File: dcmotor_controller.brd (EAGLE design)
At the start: 142.2 x 90.6 mm, 87 parts, among them IC1 L298, IC2 L298, Q1 MOSFET-PCHANNEL_SOT23-3, Q2 8MHz, T1 BC857BS, T14 BSS306N, U1 SN74LVC4245APWR, U2 STM32F10XRXT6, U3 SN74LVC4245APWR, U4 MCP1825S-3302E/DB

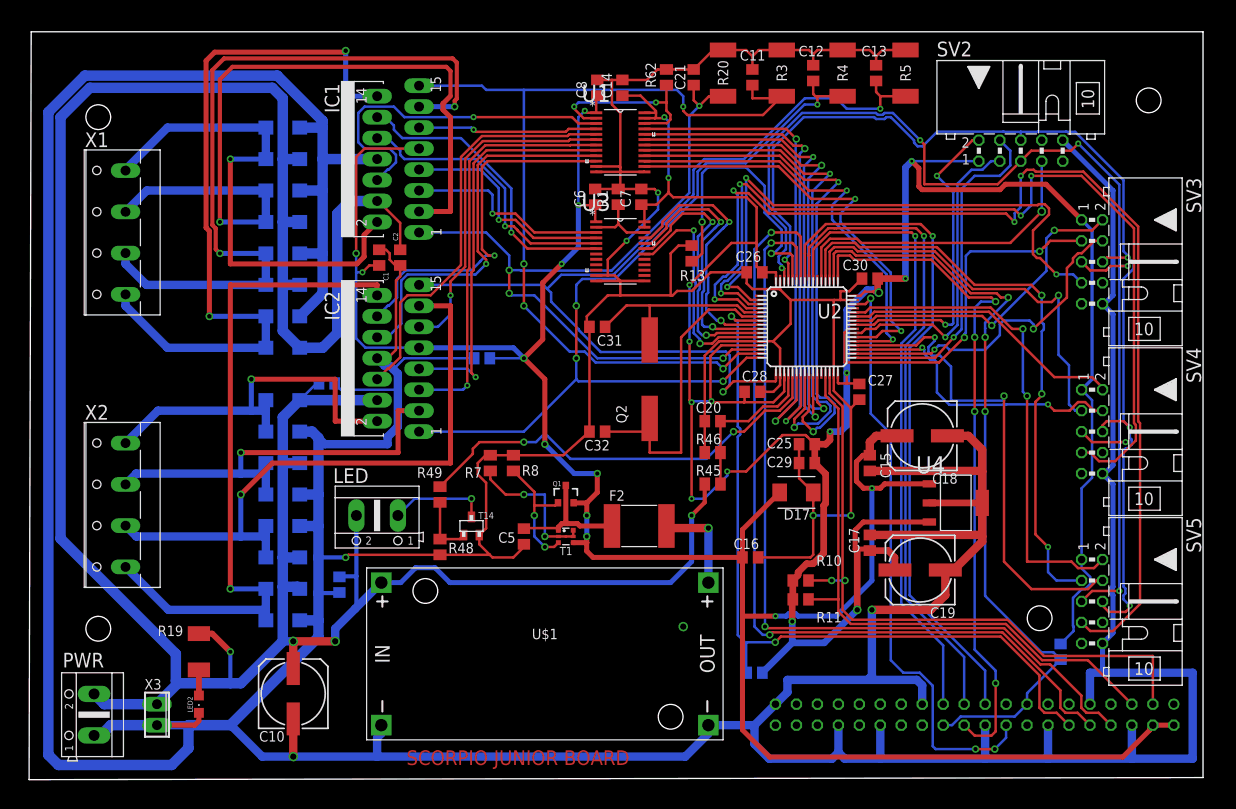
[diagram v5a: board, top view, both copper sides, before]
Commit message: renumber parts, small changes in layout
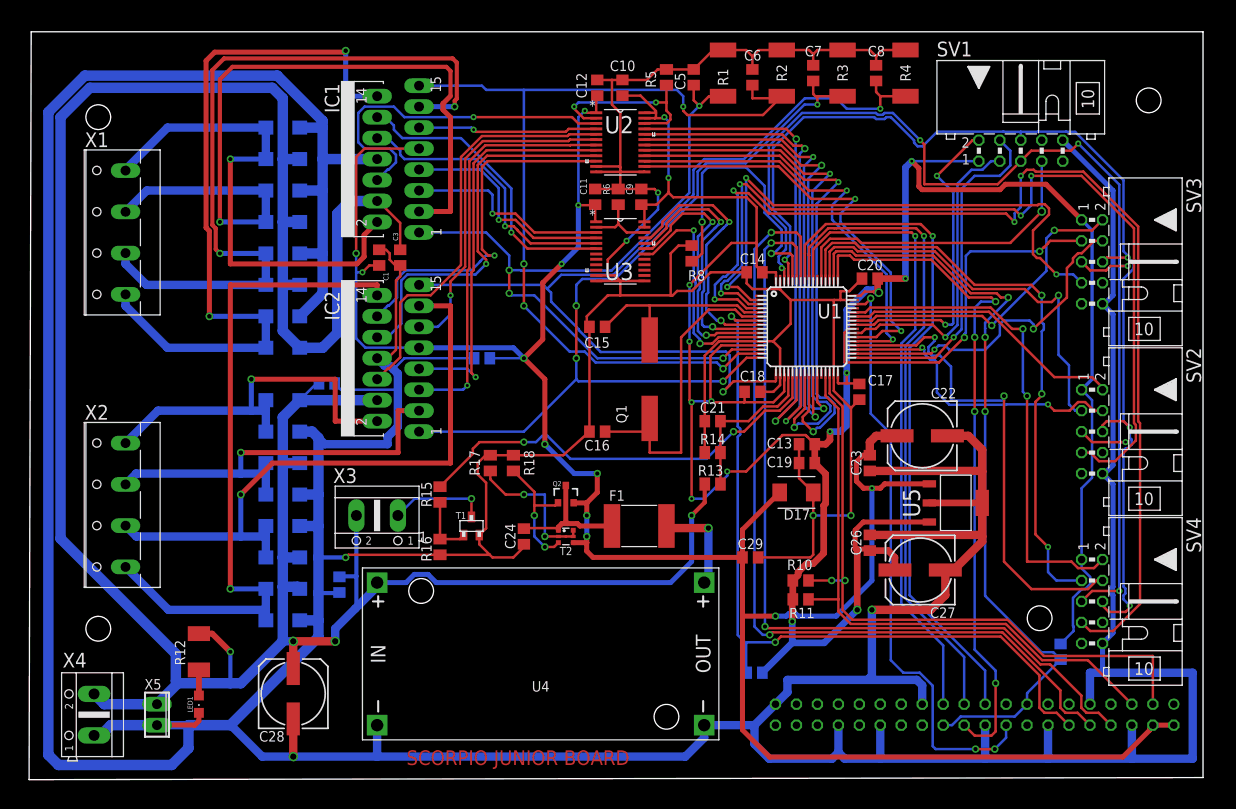
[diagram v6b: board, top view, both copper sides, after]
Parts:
- removed C30: 100n, rcl:C0805
- removed C31, C32: 20p, rcl:C0805
- removed LED: (no value), con-ptr500:AK500/2
- removed R19: 1.2k, 0.5W, rcl:R2010
- removed R20: 0R25, rcl:R2512
- removed R45, R62: 10k, resistor:M0805
- removed R46: 2k2, resistor:M0805
- removed SV6: (no value), con-lsta:FE20-2
- removed T14: BSS306N, we-transistor:SOT23
- removed U$1: DC-DC-STEP-DOWN-LM2596, lm2596:DC-DC-STEP-DOWN-LM2596
- added C22: 10u, resistor:153CLV-0807
- added C23: 100n, resistor:C0805
- added C24: (no value), rcl:C0805
- added R17, R18: 10k 1%, resistor:M0805
- added R2: 0R25, rcl:R2512
- added R6: 10k, resistor:M0805
- added R9: (no value), rcl:R0805
- added SV1: (no value), con-ml:ML10L
- added T2: BC857BS, NXP_60_26022015:SOT363
- added U5: MCP1825S-3302E/DB, MCP1825S-3302E_DB:SOT230P700X180-4N
- added X5: (no value), con-phoenix-254:2POL254
- C10: value 100u -> 100n; device resistor:153CLV-0807 -> resistor:C0805
- C13: value 100n -> 4u7; device resistor:C0805 -> rcl:C0805
- C14, C17, C3: device resistor:C0805 -> rcl:C0805
- C15, C16: value 100n -> 20p; device resistor:C0805 -> rcl:C0805
- C18: value 10u -> 100n; device resistor:153CLV-0807 -> rcl:C0805
- C19: value 10u -> 1u; device resistor:153CLV-0807 -> rcl:C0805
- C2, C25, C26: device rcl:C0805 -> resistor:C0805
- C20: value 47u -> 100n; device resistor:C0805 -> rcl:C0805
- C21: value 100n -> 47u
- C27: value 100n -> 10u; device rcl:C0805 -> resistor:153CLV-0807
- C28: value 100n -> 100u; device rcl:C0805 -> resistor:153CLV-0807
- C29: value 1u -> 100n; device rcl:C0805 -> resistor:C0805
- C5: value (none) -> 100n; device rcl:C0805 -> resistor:C0805
- C9: value 4u7 -> 100n
- Q1: value MOSFET-PCHANNEL_SOT23-3 -> 8MHz; device Simplex-DiscreteSemi:SOT23-3 -> crystal:CSM-7X-DU
- Q2: value 8MHz -> MOSFET-PCHANNEL_SOT23-3; device crystal:CSM-7X-DU -> Simplex-DiscreteSemi:SOT23-3
- R1: value 10k -> 0R25; device resistor:M0805 -> rcl:R2512
- R12: value 10k -> 1.2k, 0.5W; device rcl:R0805 -> rcl:R2010
- R13: device rcl:R0805 -> resistor:M0805
- R14: value (none) -> 2k2; device rcl:R0805 -> resistor:M0805
- R5: value 0R25 -> 10k; device rcl:R2512 -> resistor:M0805
- R7, R8: value 10k 1% -> 10k; device resistor:M0805 -> rcl:R0805
- SV5: device con-ml:ML10L -> con-lsta:FE20-2
- T1: value BC857BS -> BSS306N; device NXP_60_26022015:SOT363 -> we-transistor:SOT23
- U1: value SN74LVC4245APWR -> STM32F10XRXT6; device Texas Instruments_By_element14_Batch_1:SOP65P640X120-24N -> stm32:TQFP64
- U2: value STM32F10XRXT6 -> SN74LVC4245APWR; device stm32:TQFP64 -> Texas Instruments_By_element14_Batch_1:SOP65P640X120-24N
- U4: value MCP1825S-3302E/DB -> DC-DC-STEP-DOWN-LM2596; device MCP1825S-3302E_DB:SOT230P700X180-4N -> lm2596:DC-DC-STEP-DOWN-LM2596
- X3: device con-phoenix-254:2POL254 -> con-ptr500:AK500/2
- moved C10 83.5 mm to (71.6, 83.6)
- moved R12 67.4 mm to (20.3, 15.2), flipped to the top, turned to 270 degrees
- moved C28 66.6 mm to (31.8, 10.2), turned to 90 degrees
- moved D16 59.7 mm to (30.5, 19.1)
- moved C9 59.5 mm to (73.9, 70.4), flipped to the top, turned to 90 degrees
- moved C5 59.3 mm to (80.3, 84.8)
- moved C25 59.1 mm to (37.3, 23.4), flipped to the bottom, turned to 270 degrees
- moved U4 53.5 mm to (61.7, 15.0)
- moved R14 48.6 mm to (82.5, 39.4), flipped to the top, turned to 0 degrees
- moved D15 48.3 mm to (30.5, 22.9), turned to 0 degrees
- moved C13 45.7 mm to (94.0, 40.4), turned to 180 degrees
- moved C21 41.7 mm to (82.5, 43.2), turned to 180 degrees
- moved R7 40.9 mm to (87.6, 12.7), flipped to the bottom, turned to 180 degrees
- moved C15 36.9 mm to (68.6, 54.6), turned to 0 degrees
- moved X3 36.0 mm to (41.9, 31.8), turned to 180 degrees
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- renumbered D19 to D1, F2 to F1, LED2 to LED1, PWR to X4, R48 to R16, R49 to R15
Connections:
- net 24V: now also C25.1, C28.+, C3.1, D11.C, D13.C, D15.C, D9.C, R12.1, R13.2, U4.IN+, X3.2, X5.1; no longer C10.+, C2.1, C9.1, D2.C, D4.C, D6.C, D8.C, LED.2, R19.1, R45.2, U$1.IN+, X3.1
- net 3V3: now also C10.1, C13.1, C18.1, C19.1, C20.1, C27.+, C9.1, R7.2, R9.2, SV1.1, U1.13, U1.19, U1.32, U1.48, U1.64, U2.23, U2.24, U5.3; no longer C19.+, C25.1, C27.1, C28.1, C29.1, C30.1, C7.1, R12.2, R14.2, SV5.1, U1.23, U1.24, U2.13, U2.19, U2.32, U2.48, U2.64, U4.3
- net 5V: now also C11.1, C12.1, C2.2, C22.+, C23.1, C29.1, Q2.2, SV5.2, SV5.4, T2.4, U2.1, U5.1; no longer C15.1, C16.1, C18.+, C3.2, C6.1, C8.1, Q1.2, SV6.2, SV6.4, T1.4, U1.1, U4.1
- net A_LSB_U1: now also SV1.2, U1.41; no longer SV2.2, U2.41
- net A_LSB_U2: now also U1.42; no longer U2.42
- net A_LSB_U3: now also SV2.2, U1.43; no longer SV4.2, U2.43
- net A_LSB_U4: now also SV4.2, U1.44; no longer SV5.2, U2.44
- net BAT_MEAS: now also C21.1, R13.1, R14.2, U1.20; no longer C20.1, R45.1, R46.2, U2.20
- net BOOTO: now also R8.2, U1.60; no longer R13.2, U2.60
- net B_DIR_V1: now also SV1.3, U1.39; no longer SV2.3, U2.39
- net B_DIR_V2: now also U1.40; no longer U2.40
- net B_DIR_V3: now also SV2.3, U1.51; no longer SV4.3, U2.51
- net B_DIR_V4: now also SV4.3, U1.52; no longer SV5.3, U2.52
- net CLK: now also SV1.6, U1.61; no longer SV5.6, U2.61
- net CSN: now also SV1.5, U1.62; no longer SV5.5, U2.62
- net D01: now also SV1.7, U1.53; no longer SV2.7, U2.53
- net D02: now also U1.2; no longer U2.2
- net D03: now also SV2.7, U1.3; no longer SV4.7, U2.3
- net D04: now also SV4.7, U1.4; no longer SV5.7, U2.4
- net EN1_UC: now also U1.22, U2.21; no longer U1.21, U2.22
- net EN2_UC: now also U1.23, U2.20; no longer U1.20, U2.23
- net EN3_UC: now also U1.26, U2.19; no longer U1.19, U2.26
- net EN4_UC: now also U1.27, U2.18; no longer U1.18, U2.27
- net GND: now also C10.2, C11.2, C12.2, C13.2, C15.1, C16.1, C18.2, C19.2, C2.1, C21.2, C22.-, C23.2, C24.2, C27.-, C28.-, C3.2, C5.1, C6.1, C7.1, C8.1, D2.A, D4.A, D6.A, D8.A, R1.1, R14.1, R17.1, R18.1, R2.1, R5.2, R6.2, SV1.10, SV5.14, SV5.20, SV5.25, SV5.30, SV5.34, SV5.39, SV5.6, SV5.9, T1.2, U1.18, U1.31, U1.47, U1.63, U2.11, U2.13, U4.IN-, U4.OUT-, U5.2, U5.4, X5.2; no longer C10.-, C11.1, C12.1, C13.1, C15.2, C16.2, C18.-, C19.-, C2.2, C21.1, C27.2, C28.2, C3.1, C30.2, C31.1, C32.1, C5.2, C6.2, C7.2, C8.2, D11.A, D13.A, D15.A, D9.A, R1.2, R13.1, R20.1, R46.1, R5.1, R62.2, R7.1, SV5.10, SV6.14, SV6.20, SV6.25, SV6.30, SV6.34, SV6.39, SV6.6, SV6.9, T14.2, U$1.IN-, U$1.OUT-, U1.11, U1.13, U2.18, U2.31, U2.47, U2.63, U4.2, U4.4, X3.2
- net IN11_UC: now also U1.8; no longer U2.8
- net IN12_UC: now also U1.9; no longer U2.9
- net IN21_UC: now also U1.10; no longer U2.10
- net IN22_UC: now also U1.11; no longer U2.11
- net IN31: now also U2.7; no longer U1.7
- net IN31_UC: now also U1.24, U2.17; no longer U1.17, U2.24
- net IN32: now also U2.8; no longer U1.8
- net IN32_UC: now also U1.25, U2.16; no longer U1.16, U2.25
- net IN41: now also U2.9; no longer U1.9
- net IN41_UC: now also U1.37, U2.15; no longer U1.15, U2.37
- net IN42: now also U2.10; no longer U1.10
- net IN42_UC: now also U1.38, U2.14; no longer U1.14, U2.38
- net INDEX_W1: now also SV1.4, U1.33; no longer SV2.4, U2.33
- net INDEX_W2: now also U1.34; no longer U2.34
- net INDEX_W3: now also SV2.4, U1.35; no longer SV4.4, U2.35
- net INDEX_W4: now also SV4.4, U1.36; no longer SV5.4, U2.36
- net LED: now also U1.21; no longer U2.21
- net MOT11: now also D2.C; no longer D16.C
- net MOT12: now also D3.A, D4.C; no longer D15.C, D2.A
- net MOT21: now also D5.A, D6.C; no longer D14.C, D3.A
- net MOT22: now also D7.A, D8.C; no longer D13.C, D4.A
- net MOT31: now also D10.C, D9.A; no longer D12.C, D5.A
- net MOT32: now also D11.A, D12.C; no longer D11.C, D6.A
- net MOT41: now also D13.A, D14.C; no longer D10.C, D7.A
- net MOT42: now also D15.A, D16.C; no longer D8.A, D9.C
- net N$1: now also U4.OUT+; no longer U$1.OUT+
- net N$16: now also U1.1; no longer U2.1
- net N$19: now also Q2.1, R18.2, T2.3; no longer Q1.1, R8.2, T1.3
- net N$20: now also R17.2, T2.2, T2.5, T2.6; no longer R7.2, T1.2, T1.5, T1.6
- net N$21: now also T1.1; no longer T14.1
- net N$24: now also T1.3, X3.1; no longer LED.1, T14.3
- net N$3: now also R12.2; no longer R19.2
- net N$4: now also R5.1, U2.2, U2.22; no longer R62.1, U1.2, U1.22
- net N$5: now also R6.1; no longer R1.1
- net N$6: now also C24.1, Q2.3, T2.1; no longer C5.1, Q1.3, T1.1
- net NRST: now also R7.1, SV5.12, U1.7; no longer R12.1, SV6.12, U2.7
- net OSC_IN: now also C15.2, Q1.2, U1.5; no longer C31.2, Q2.2, U2.5
- net OSC_OUT: now also C16.2, Q1.1, U1.6; no longer C32.2, Q2.1, U2.6
- net PWM1: now also SV1.9; no longer SV2.9
- net PWM3: now also SV2.9; no longer SV4.9
- net PWM4: now also SV4.9; no longer SV5.9
- net PWM_F1: now also SV1.8; no longer SV2.8
- net PWM_F3: now also SV2.8; no longer SV4.8
- net PWM_F4: now also SV4.8; no longer SV5.8
- net PWM_SIGNAL1: now also U2.3; no longer U1.3
- net PWM_SIGNAL2: now also U2.4; no longer U1.4
- net PWM_SIGNAL3: now also U2.5; no longer U1.5
- net PWM_SIGNAL4: now also U2.6; no longer U1.6
- net RPI_CLK: now also SV5.23, U1.55; no longer SV6.23, U2.55
- net RPI_MISO: now also SV5.21, U1.56; no longer SV6.21, U2.56
- net RPI_MOSI: now also SV5.19, U1.57; no longer SV6.19, U2.57
- net RPI_RXD: now also SV5.10, U1.58; no longer SV6.10, U2.58
- net RPI_TXD: now also SV5.8, U1.59; no longer SV6.8, U2.59
- net SCL: now also SV5.5, U1.29; no longer SV6.5, U2.29
- net SDA: now also SV5.3, U1.30; no longer SV6.3, U2.30
- net SEN1: now also C5.2, R1.2, U1.14; no longer C21.2, R20.2, U2.14
- net SEN2: now also C6.2, R2.2, U1.15; no longer C11.2, R3.2, U2.15
- net SEN3: now also C7.2, R3.2, U1.16; no longer C12.2, R4.2, U2.16
- net SEN4: now also C8.2, R4.2, U1.17; no longer C13.2, R5.2, U2.17
- net SPI1_NSS: now also R9.1, SV5.15, SV5.24, U1.50; no longer R14.1, SV6.15, SV6.24, U2.50
- net SWCLK: now also SV5.22, U1.49; no longer SV6.22, U2.49
- net SWDIO: now also SV5.18, U1.46; no longer SV6.18, U2.46
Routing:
- net GND: track 967.4 -> 966.4 mm

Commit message: Add files via upload
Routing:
- net GND: track 966.4 -> 158.1 mm, vias 7 -> 2
